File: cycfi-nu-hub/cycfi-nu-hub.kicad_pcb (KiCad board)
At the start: 2 copper layers, 61 x 24 mm, 18 parts, among them J1 TO BREAKOUT J3, P1 CH1 PWR, P2 CH2 PWR, P3 CH3 PWR, P4 CH4 PWR, P5 CH5 PWR, P6 CH6 PWR

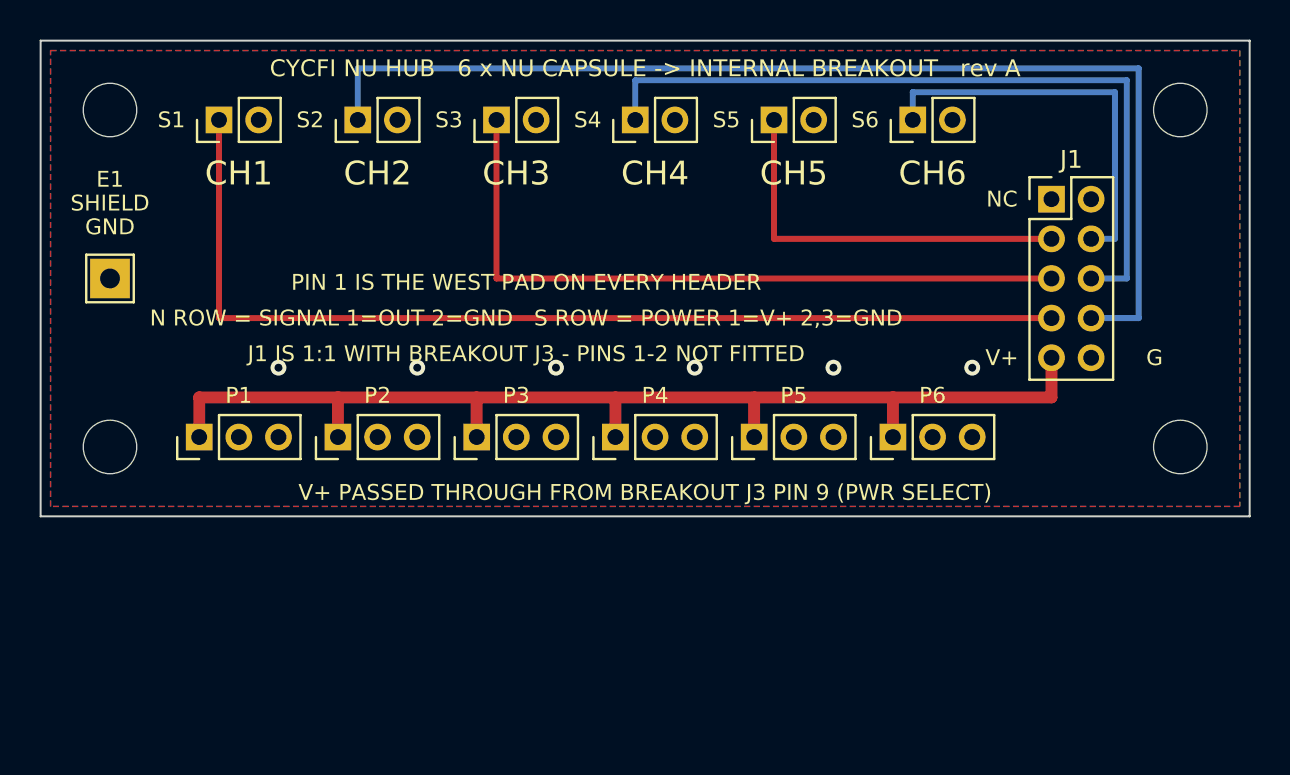
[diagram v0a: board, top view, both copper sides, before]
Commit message: Match the Internal Breakout's outline and hole pattern
The hub was a 61 x 24 mm strip of its own choosing. It is now 50 x 35 mm with
1.75 mm corners and four M2 holes on 45 x 30 mm centres -- the breakout's own
geometry -- so one mount, one cavity cut-out or one enclosure pocket takes
either board.

Every number is measured off Cycfi's internal_breakout.brd (Eagle layer 20)
and lives in design.MOUNTING_PATTERN; gen_pcb.py derives its dimensions from
there and asserts the hole centres against it. Two figures are deliberately
regularised rather than transcribed, and both are recorded: Cycfi's four hole
centres are not quite a rectangle (29.9 vs 30.0 mm, insets 2.52 to 2.55), and
their four corner arcs do not share a radius (three at ~1.77, one at 1.63).

Also corrects a misattribution in the docs. They stated Cycfi list breakout
v2.6 as 27 x 38 mm; that figure is prose from the Nu Series *v1* page and
names no version. The v2.6.1 datasheet carries no dimensions at all and
neither does the 2023 redesign announcement, so 50 x 35 is the only measured
breakout outline in existence -- and it is v2.5's. That assumption now travels
with the geometry in fab/*-mechanical.json rather than living only in prose.

Three things fell out of the smaller outline:

- The fan-in had to be re-derived. The lanes stay north of the signal row, and
  check_placement() now asserts the lane order and descent order are reverses
  of each other -- the property that was violated when the middle band looked
  like the obvious home for them.
- check_holes_clear() is new. At 2.5 mm in from all four edges the holes now
  sit in the margin the descents run down, and an unplated hole has no pad, no
  net and no courtyard, so nothing else here would notice a track across one.
- check_fits() tests courtyard polygons against the rounded outline. Bounding
  boxes falsely reported all four holes as overhanging a board they fit.

ERC 0, DRC 0 (warnings included), netlist matches design.py.

Co-Authored-By: C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
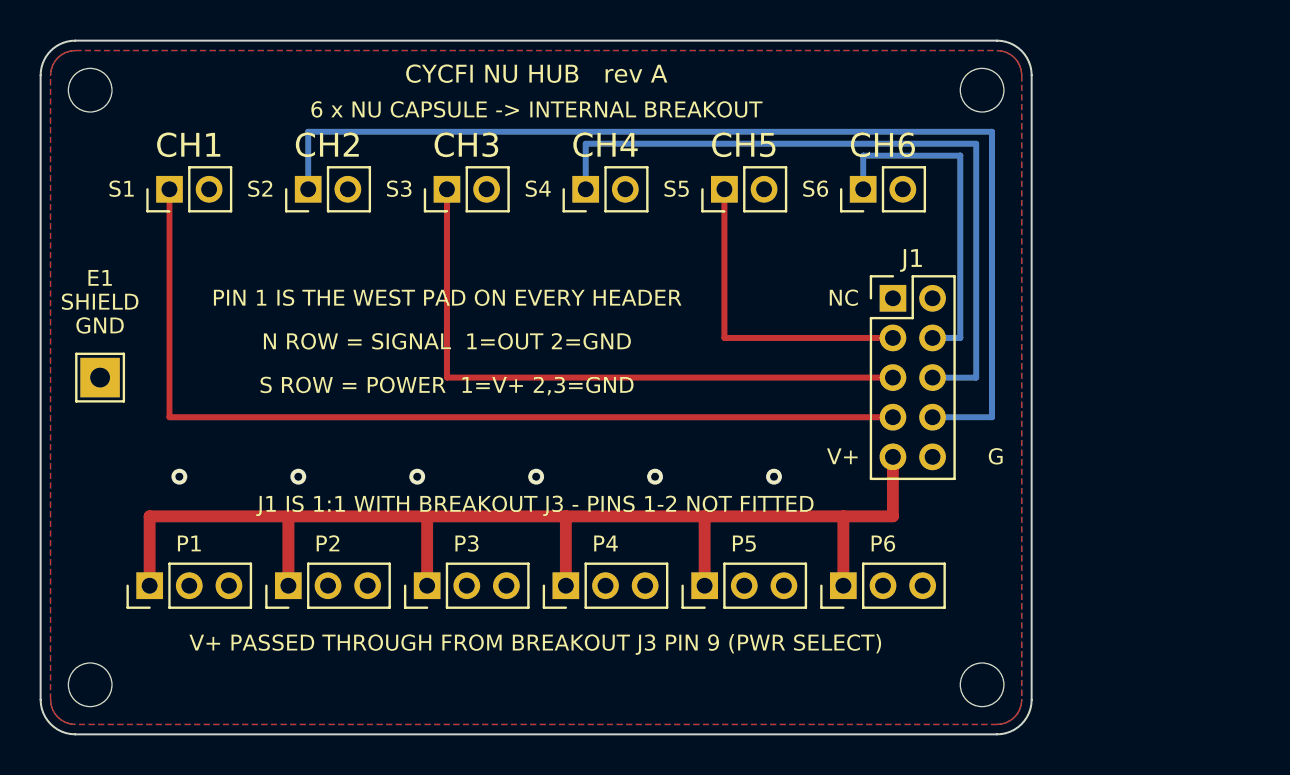
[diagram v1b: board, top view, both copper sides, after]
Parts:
- H1, H2, H3, H4: value M2.5 -> M2; footprint MountingHole:MountingHole_2.7mm_M2.5 -> MountingHole:MountingHole_2.2mm_M2
- moved H4 15.6 mm to (47.5, 32.5)
- moved H2 12.0 mm to (2.50, 32.5)
- moved H3 10.0 mm to (47.5, 2.50)
- moved J1 9.43 mm to (43.0, 13.0)
- moved P1 7.91 mm to (5.50, 27.5)
- moved P2 7.91 mm to (12.5, 27.5)
- moved P3 7.91 mm to (19.5, 27.5)
- moved P4 7.91 mm to (26.5, 27.5)
- moved P5 7.91 mm to (33.5, 27.5)
- moved P6 7.91 mm to (40.5, 27.5)
- moved E1 5.02 mm to (3.00, 17.0)
- moved S1 4.30 mm to (6.50, 7.50)
- moved S2 4.30 mm to (13.5, 7.50)
- moved S3 4.30 mm to (20.5, 7.50)
- moved S4 4.30 mm to (27.5, 7.50)
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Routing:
- net V+: track 57.0 -> 61.5 mm
- net CH5: track 20.0 -> 16.0 mm
- net CH3: track 36.0 -> 32.0 mm
- net CH1: track 52.0 -> 48.0 mm
- net CH6: track 20.2 -> 17.2 mm
- net CH4: track 38.6 -> 36.0 mm
- net CH2: track 57.0 -> 54.8 mm
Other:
- board size 61 x 24 mm -> 50 x 35 mm
- board text added: "6 x NU CAPSULE -> INTERNAL BREAKOUT"
- board text added: "CYCFI NU HUB rev A"
- board text added: "N ROW = SIGNAL 1=OUT 2=GND"
- board text added: "S ROW = POWER 1=V+ 2,3=GND"
- board text removed: "CYCFI NU HUB 6 x NU CAPSULE -> INTERNAL BREAKOUT rev A"
- board text removed: "N ROW = SIGNAL 1=OUT 2=GND S ROW = POWER 1=V+ 2,3=GND"
